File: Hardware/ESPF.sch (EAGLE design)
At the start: 25 parts, among them IC1 CP2102N-A01-GQFN24, J1 USB-C-16P-16P, J2 ESPFLASH-1X6-2.54-PINS-RA, Q1 MMDT3904

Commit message: Wurth_Connectors_WR-USB
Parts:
- added J3: 629722000214, Wurth_Connectors_WR-USB:629722000214
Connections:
- removed net VIN: F1.1, J1.VBUS
- new net +5V: J3.VBUS, J3.VBUS1, J3.VBUS2, J3.VBUS3
- net 5V: now also F1.1, J1.VBUS
- net D+: now also J3.D-1, J3.D-2
- net D-: now also J3.D+1, J3.D+2
- net GND: now also J3.GND, J3.GND1, J3.GND2, J3.GND3
- net N$10: now also J3.CC1
- net N$9: now also J3.CC2
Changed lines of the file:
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@@
 <setting verticaltext="up"/>
 </settings>
-<grid distance="0.1" unitdist="inch" unit="inch" style="lines" multiple="1" display="no" altdistance="0.01" altunitdist="inch" altunit="inch"/>
+<grid distance="0.05" unitdist="inch" unit="inch" style="lines" multiple="1" display="yes" altdistance="0.01" altunitdist="inch" altunit="inch"/>
 <layers>
 <layer number="1" name="Top" color="4" fill="1" visible="no" active="no"/>
@@
 <part name="C3" library="SuperHouse-DiscreteSemi" library_urn="urn:adsk.eagle:library:11768461" deviceset="CAP" device="0603" package3d_urn="urn:adsk.eagle:package:7066315/6" value="100nF"/>
 <part name="GND10" library="SuperHouse-SupplySymbols" library_urn="urn:adsk.eagle:library:11790503" deviceset="GND" device=""/>
+<part name="J3" library="Wurth_Connectors_WR-USB" library_urn="urn:adsk.eagle:library:16513831" deviceset="629722000214" device="" package3d_urn="urn:adsk.eagle:package:32827710/4" value="629722000214"/>
+<part name="GND11" library="supply1" library_urn="urn:adsk.eagle:library:371" deviceset="GND" device=""/>
+<part name="GND12" library="supply1" library_urn="urn:adsk.eagle:library:371" deviceset="GND" device=""/>
+<part name="P+5" library="supply1" library_urn="urn:adsk.eagle:library:371" deviceset="+5V" device=""/>
+<part name="P+6" library="supply1" library_urn="urn:adsk.eagle:library:371" deviceset="+5V" device=""/>
 </parts>
 <sheets>
@@
 <attribute name="VALUE" x="193.04" y="91.44" size="1.778" layer="96"/>
 </instance>
+<instance part="J3" gate="G$1" x="-27.94" y="111.76" smashed="yes">
+<attribute name="NAME" x="-27.94" y="123.19" size="1.6764" layer="95" align="bottom-center"/>
+<attribute name="VALUE" x="-27.94" y="96.52" size="1.6764" layer="96" align="bottom-center"/>
+</instance>
+<instance part="GND11" gate="1" x="-53.34" y="93.98" smashed="yes">
+<attribute name="VALUE" x="-55.88" y="91.44" size="1.778" layer="96"/>
+</instance>
+<instance part="GND12" gate="1" x="-2.54" y="93.98" smashed="yes">
+<attribute name="VALUE" x="-5.08" y="91.44" size="1.778" layer="96"/>
+</instance>
+<instance part="P+5" gate="1" x="-50.8" y="132.08" smashed="yes">
+<attribute name="VALUE" x="-53.34" y="127" size="1.778" layer="96" rot="R90"/>
+</instance>
+<instance part="P+6" gate="1" x="-5.08" y="132.08" smashed="yes">
+<attribute name="VALUE" x="-7.62" y="127" size="1.778" layer="96" rot="R90"/>
+</instance>
 </instances>
 <busses>
@@
 <pinref part="F1" gate="A" pin="2"/>
 <wire x1="63.5" y1="121.92" x2="48.26" y2="121.92" width="0.1524" layer="91"/>
+<pinref part="F1" gate="A" pin="1"/>
+<pinref part="J1" gate="G$1" pin="VBUS"/>
+<wire x1="27.94" y1="121.92" x2="38.1" y2="121.92" width="0.1524" layer="91"/>
+<wire x1="38.1" y1="121.92" x2="48.26" y2="121.92" width="0.1524" layer="91"/>
+<junction x="38.1" y="121.92"/>
+<junction x="48.26" y="121.92"/>
 </segment>
 <segment>
@@
 <wire x1="195.58" y1="96.52" x2="195.58" y2="104.14" width="0.1524" layer="91"/>
 </segment>
+<segment>
+<pinref part="J3" gate="G$1" pin="GND"/>
+<wire x1="-43.18" y1="119.38" x2="-53.34" y2="119.38" width="0.1524" layer="91"/>
+<wire x1="-53.34" y1="119.38" x2="-53.34" y2="101.6" width="0.1524" layer="91"/>
+<pinref part="GND11" gate="1" pin="GND"/>
+<pinref part="J3" gate="G$1" pin="GND1"/>
+<wire x1="-53.34" y1="101.6" x2="-53.34" y2="96.52" width="0.1524" layer="91"/>
+<wire x1="-43.18" y1="101.6" x2="-53.34" y2="101.6" width="0.1524" layer="91"/>
+<junction x="-53.34" y="101.6"/>
+</segment>
+<segment>
+<pinref part="J3" gate="G$1" pin="GND2"/>
+<wire x1="-12.7" y1="119.38" x2="-2.54" y2="119.38" width="0.1524" layer="91"/>
+<wire x1="-2.54" y1="119.38" x2="-2.54" y2="101.6" width="0.1524" layer="91"/>
+<pinref part="GND12" gate="1" pin="GND"/>
+<pinref part="J3" gate="G$1" pin="GND3"/>
+<wire x1="-2.54" y1="101.6" x2="-2.54" y2="96.52" width="0.1524" layer="91"/>
+<wire x1="-12.7" y1="101.6" x2="-2.54" y2="101.6" width="0.1524" layer="91"/>
+<junction x="-2.54" y="101.6"/>
+</segment>
 </net>
 <net name="D-" class="0">
@@
 <pinref part="J1" gate="G$1" pin="D-"/>
 <wire x1="27.94" y1="114.3" x2="60.96" y2="114.3" width="0.1524" layer="91"/>
+<pinref part="J3" gate="G$1" pin="D+2"/>
+<wire x1="-12.7" y1="109.22" x2="-26.67" y2="109.22" width="0.1524" layer="91"/>
+<wire x1="-26.67" y1="109.22" x2="-29.21" y2="111.76" width="0.1524" layer="91"/>
+<pinref part="J3" gate="G$1" pin="D+1"/>
+<wire x1="-29.21" y1="111.76" x2="-43.18" y2="111.76" width="0.1524" layer="91"/>
+<wire x1="27.94" y1="114.3" x2="-12.7" y2="109.22" width="0.1524" layer="91"/>
+<junction x="27.94" y="114.3"/>
+<junction x="-12.7" y="109.22"/>
 </segment>
 </net>
@@
 <pinref part="J1" gate="G$1" pin="D+"/>
 <wire x1="68.58" y1="116.84" x2="27.94" y2="116.84" width="0.1524" layer="91"/>
+<pinref part="J3" gate="G$1" pin="D-1"/>
+<wire x1="-43.18" y1="109.22" x2="-29.21" y2="109.22" width="0.1524" layer="91"/>
+<pinref part="J3" gate="G$1" pin="D-2"/>
+<wire x1="-12.7" y1="111.76" x2="-26.67" y2="111.76" width="0.1524" layer="91"/>
+<wire x1="-26.67" y1="111.76" x2="-29.21" y2="109.22" width="0.1524" layer="91"/>
+<wire x1="-12.7" y1="111.76" x2="27.94" y2="116.84" width="0.1524" layer="91"/>
+<junction x="-12.7" y="111.76"/>
+<junction x="27.94" y="116.84"/>
 </segment>
 </net>
@@
 </segment>
 </net>
-<net name="VIN" class="0">
-<segment>
-<pinref part="F1" gate="A" pin="1"/>
-<pinref part="J1" gate="G$1" pin="VBUS"/>
-<wire x1="27.94" y1="121.92" x2="38.1" y2="121.92" width="0.1524" layer="91"/>
-</segment>
-</net>
 <net name="N$6" class="0">
 <segment>
@@
 <wire x1="27.94" y1="101.6" x2="40.64" y2="101.6" width="0.1524" layer="91"/>
 <wire x1="40.64" y1="101.6" x2="40.64" y2="99.06" width="0.1524" layer="91"/>
+<pinref part="J3" gate="G$1" pin="CC2"/>
+<wire x1="-12.7" y1="106.68" x2="10.16" y2="115.57" width="0.1524" layer="91"/>
+<wire x1="10.16" y1="115.57" x2="27.94" y2="101.6" width="0.1524" layer="91"/>
+<junction x="27.94" y="101.6"/>
 </segment>
 </net>
@@
 <wire x1="27.94" y1="104.14" x2="50.8" y2="104.14" width="0.1524" layer="91"/>
 <wire x1="50.8" y1="104.14" x2="50.8" y2="99.06" width="0.1524" layer="91"/>
-</segment>
-</net>
+<pinref part="J3" gate="G$1" pin="CC1"/>
+<wire x1="27.94" y1="104.14" x2="-1.27" y2="128.27" width="0.1524" layer="91"/>
+<wire x1="-1.27" y1="128.27" x2="-43.18" y2="114.3" width="0.1524" layer="91"/>
+<junction x="27.94" y="104.14"/>
+</segment>
+</net>
+<net name="+5V" class="0">
+<segment>
+<pinref part="J3" gate="G$1" pin="VBUS"/>
+<wire x1="-50.8" y1="116.84" x2="-43.18" y2="116.84" width="0.1524" layer="91"/>
+<pinref part="J3" gate="G$1" pin="VBUS1"/>
+<wire x1="-43.18" y1="104.14" x2="-50.8" y2="104.14" width="0.1524" layer="91"/>
+<wire x1="-50.8" y1="104.14" x2="-50.8" y2="116.84" width="0.1524" layer="91"/>
+<wire x1="-50.8" y1="116.84" x2="-50.8" y2="129.54" width="0.1524" layer="91"/>
+<junction x="-50.8" y="116.84"/>
+<pinref part="P+5" gate="1" pin="+5V"/>
+</segment>
+<segment>
+<pinref part="J3" gate="G$1" pin="VBUS3"/>
+<wire x1="-12.7" y1="104.14" x2="-5.08" y2="104.14" width="0.1524" layer="91"/>
+<wire x1="-5.08" y1="104.14" x2="-5.08" y2="116.84" width="0.1524" layer="91"/>
+<pinref part="J3" gate="G$1" pin="VBUS2"/>
+<wire x1="-5.08" y1="116.84" x2="-5.08" y2="129.54" width="0.1524" layer="91"/>
+<wire x1="-12.7" y1="116.84" x2="-5.08" y2="116.84" width="0.1524" layer="91"/>
+<junction x="-5.08" y="116.84"/>
+<pinref part="P+6" gate="1" pin="+5V"/>
+</segment>
+</net>

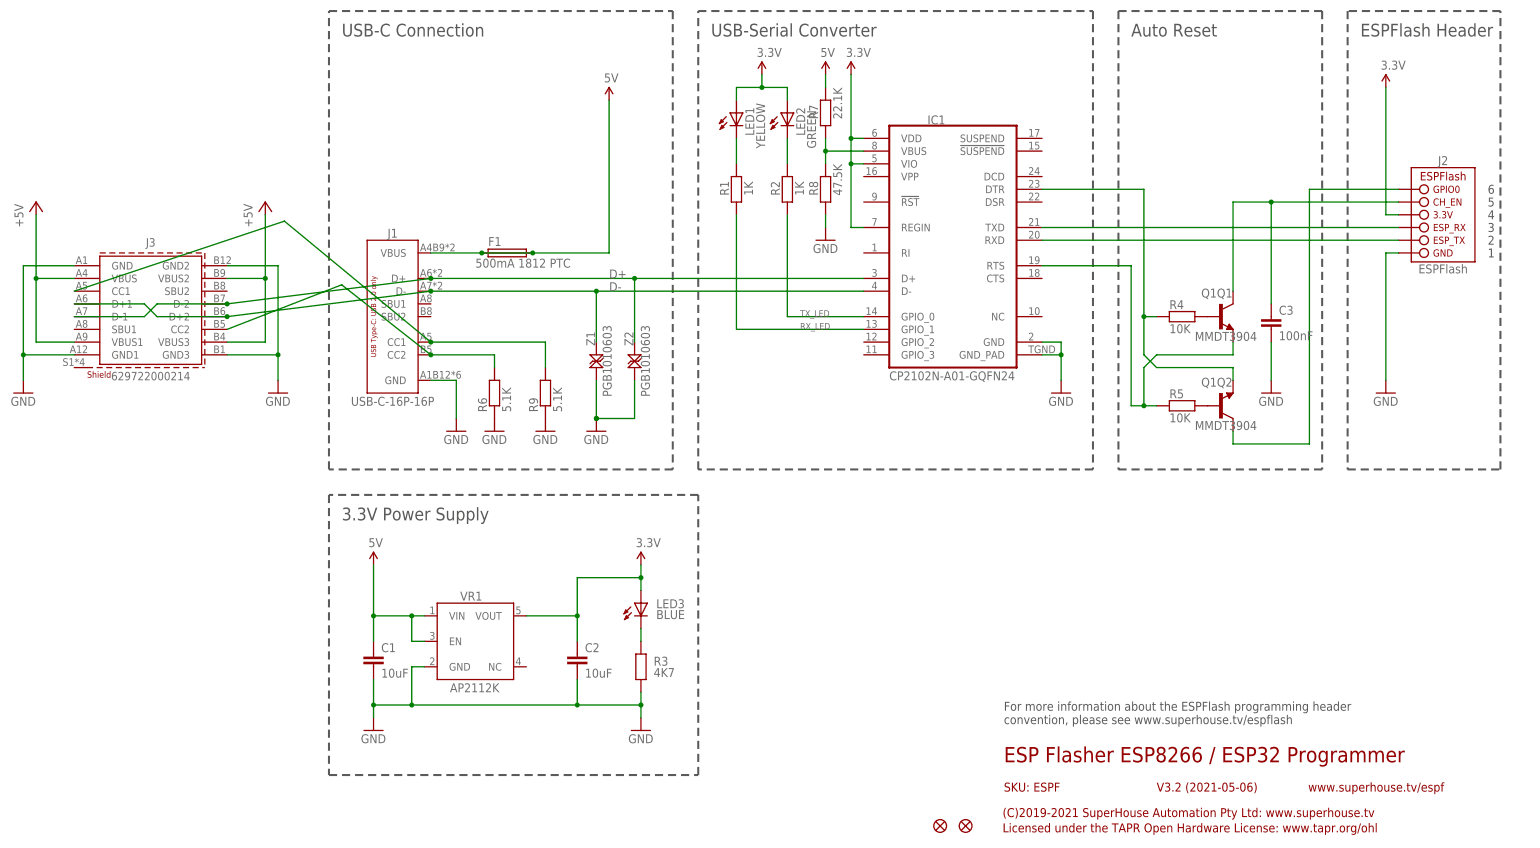
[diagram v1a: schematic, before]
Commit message: With Würht Connectors.
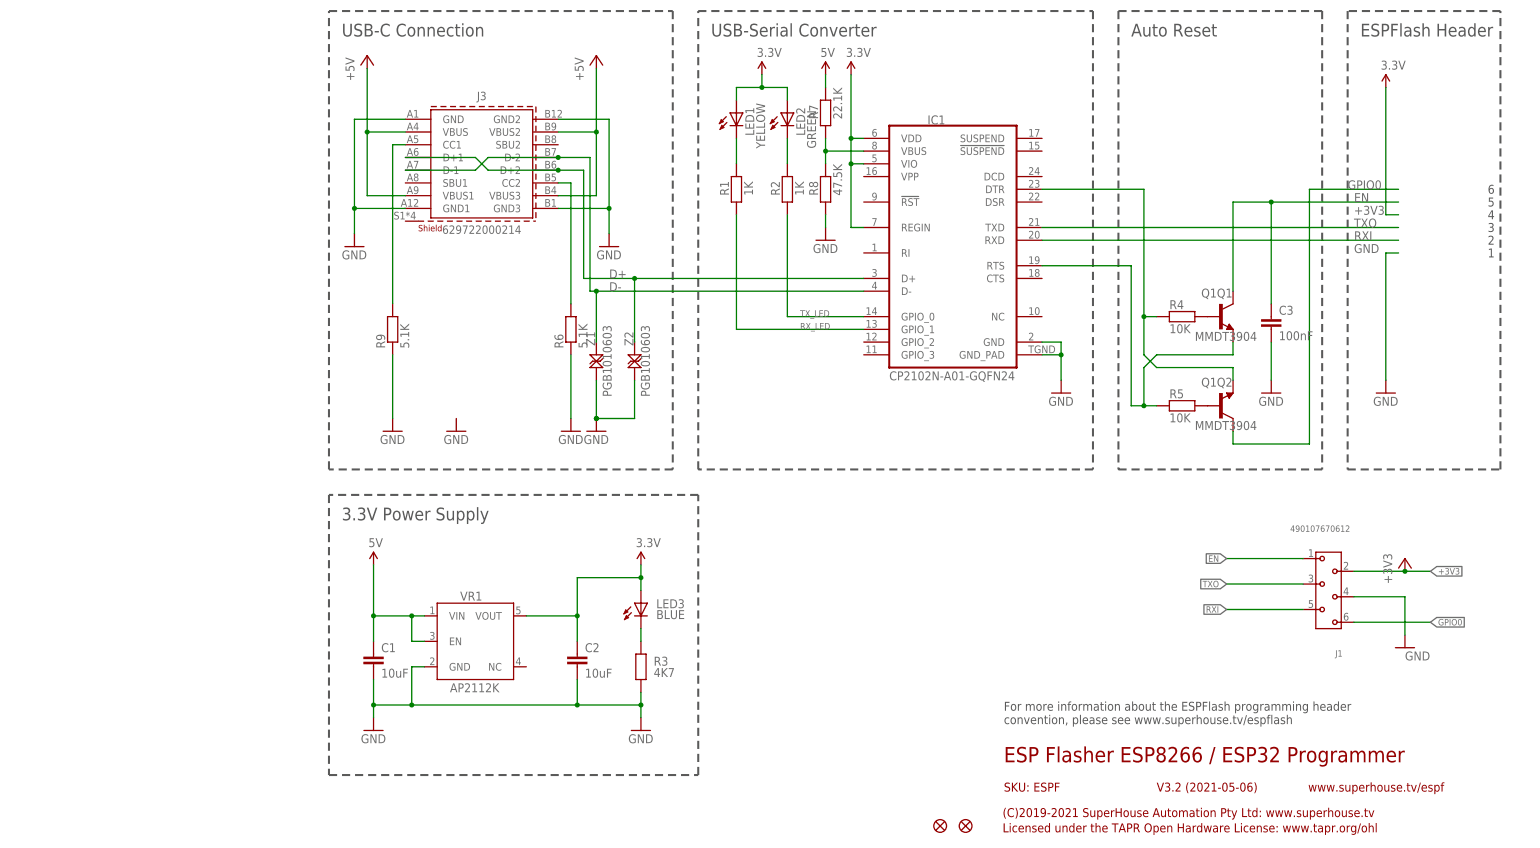
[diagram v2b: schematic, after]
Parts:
- removed F1: 500mA 1812 PTC, SuperHouse-Fuses:PTC050
- removed J2: ESPFLASH-1X6-2.54-PINS-RA, SuperHouse-ESPFlash:ESPFLASH-1X6-2.54-PINS-RA
- J1: value USB-C-16P-16P -> 490107670612; device SuperHouse-Connectors:USB-C-16P-16P -> Wurth_Connectors_WR-WST:490107670612_DEBUGGING
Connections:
- removed net 3.3V: C2.1, IC1.REGIN, IC1.VDD, IC1.VIO, J2.3.3V, LED1.A, LED2.A, LED3.A, VR1.VOUT
- removed net 5V: C1.1, F1.1, F1.2, J1.VBUS, R7.2, VR1.EN, VR1.VIN
- new net +3V3: C2.1, IC1.REGIN, IC1.VDD, IC1.VIO, J1.2, LED1.A, LED2.A, LED3.A, VR1.VOUT
- net +5V: now also C1.1, R7.2, VR1.EN, VR1.VIN
- net D+: now also J3.D+1, J3.D+2; no longer J1.D+, J3.D-1, J3.D-2
- net D-: now also J3.D-1, J3.D-2; no longer J1.D-, J3.D+1, J3.D+2
- net EN: now also J1.1; no longer J2.CH_EN
- net GND: now also J1.4; no longer J1.GND, J2.GND
- net GPIO0: now also J1.6; no longer J2.GPIO0
- net N$10: no longer J1.CC1
- net N$9: no longer J1.CC2
- net RXI: now also J1.5; no longer J2.ESP_TX
- net TXO: now also J1.3; no longer J2.ESP_RX
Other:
- moved on the sheet: J3, R6, R9
